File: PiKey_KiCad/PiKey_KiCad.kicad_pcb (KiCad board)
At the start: 2 copper layers, 22 x 42 mm, 1 part

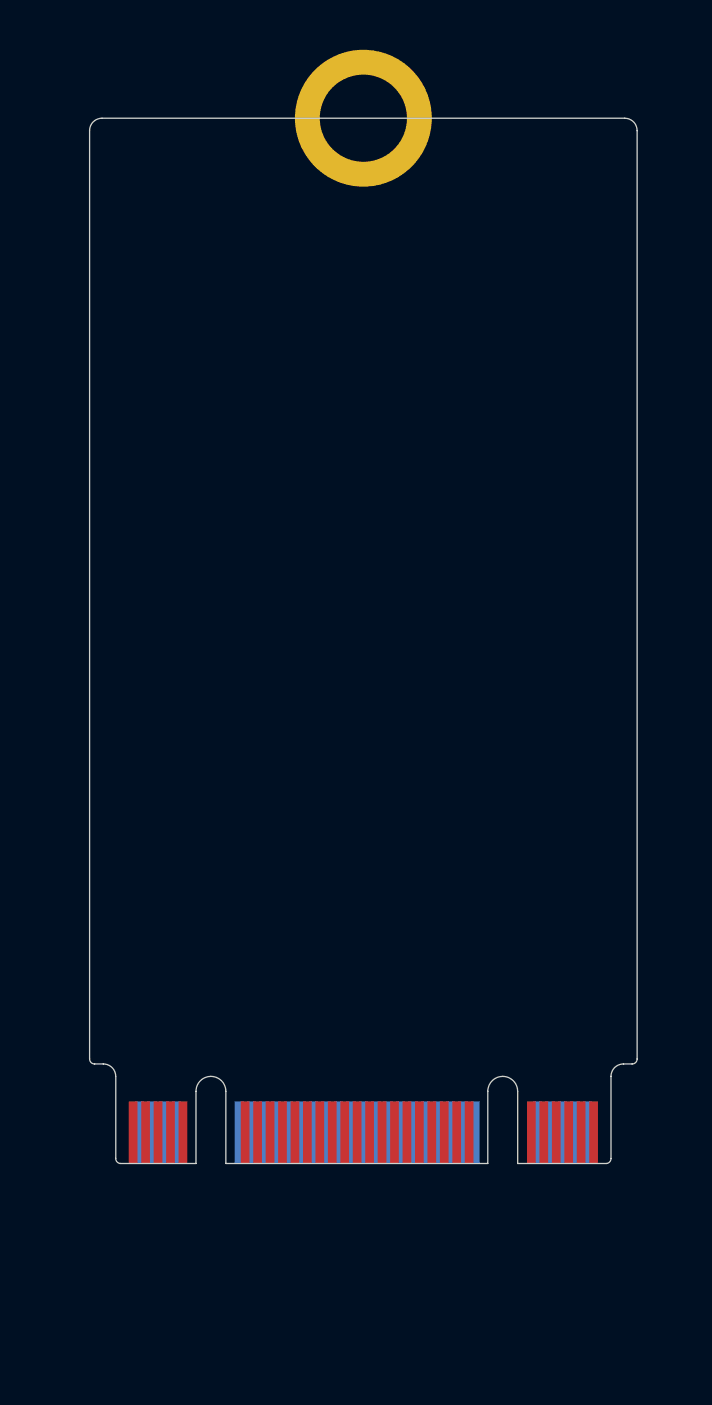
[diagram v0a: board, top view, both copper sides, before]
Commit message: Initial routing
Need to finish routing power and connecting GNDs together.
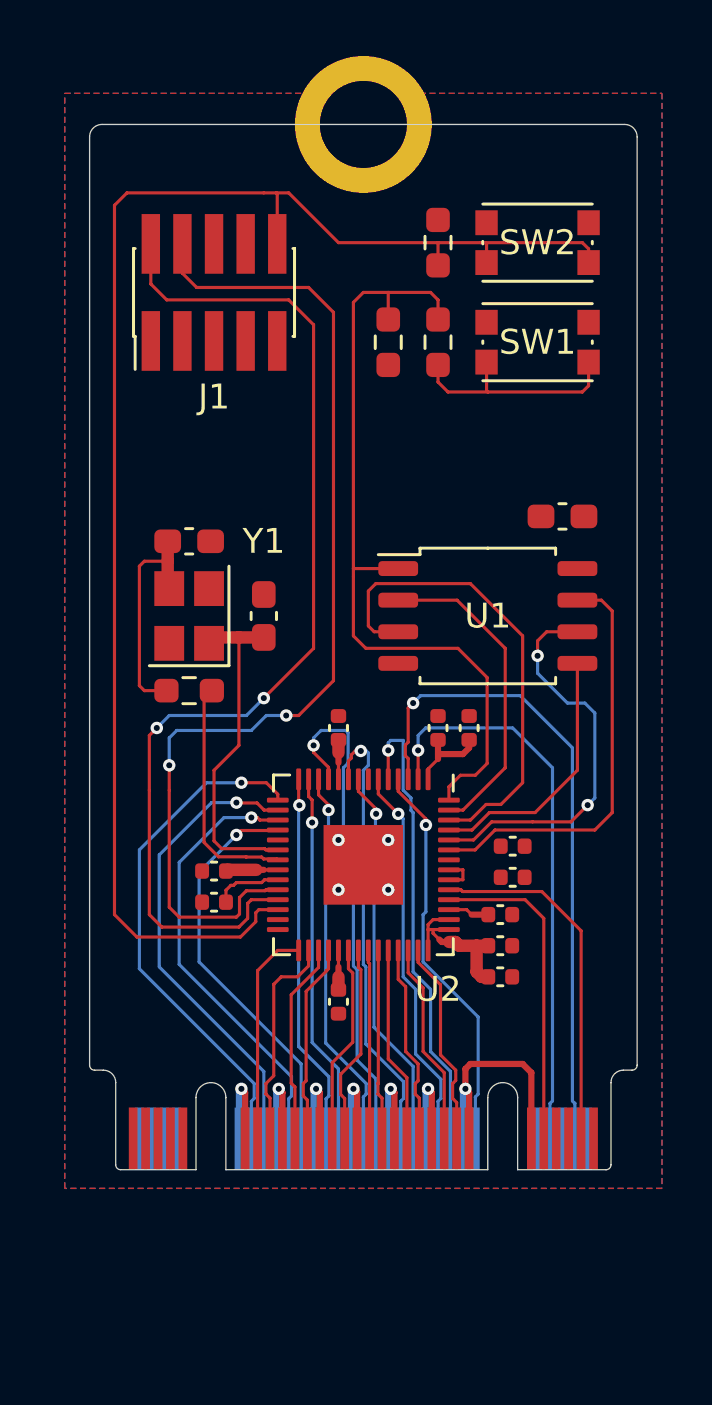
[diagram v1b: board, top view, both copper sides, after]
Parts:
- added C1: 100n, Capacitor_SMD:C_0603_1608Metric_Pad1.08x0.95mm_HandSolder, F.Cu at (158.0, 96.0)
- added C10: 100n, Capacitor_SMD:C_0402_1005Metric, F.Cu at (153.0, 104.5)
- added C11: 100n, Capacitor_SMD:C_0402_1005Metric, F.Cu at (155.5, 114.5)
- added C12: 100n, Capacitor_SMD:C_0402_1005Metric, F.Cu at (155.5, 113.2)
- added C13: 100n, Capacitor_SMD:C_0402_1005Metric, F.Cu at (156.0, 110.5)
- added C14: 100n, Capacitor_SMD:C_0402_1005Metric, F.Cu at (154.2, 104.5)
- added C2: 27p, Capacitor_SMD:C_0603_1608Metric_Pad1.08x0.95mm_HandSolder, F.Cu at (146.0, 100.0)
- added C3: 27p, Capacitor_SMD:C_0603_1608Metric_Pad1.08x0.95mm_HandSolder, F.Cu at (143.0, 97.0)
- added C4: 100n, Capacitor_SMD:C_0402_1005Metric, F.Cu at (156.0, 109.2)
- added C5: 100n, Capacitor_SMD:C_0402_1005Metric, F.Cu at (155.5, 112.0)
- added C6: 1u, Capacitor_SMD:C_0402_1005Metric, F.Cu at (144.0, 111.5)
- added C7: 1u, Capacitor_SMD:C_0402_1005Metric, F.Cu at (149.0, 115.5)
- added C8: 100n, Capacitor_SMD:C_0402_1005Metric, F.Cu at (144.0, 110.2)
- added C9: 100n, Capacitor_SMD:C_0402_1005Metric, F.Cu at (149.0, 104.5)
- added J1: SWD Header, Connector_PinHeader_1.27mm:PinHeader_2x05_P1.27mm_Vertical_SMD, F.Cu at (144.0, 87.0)
- added R1: 1K, Resistor_SMD:R_0603_1608Metric_Pad0.98x0.95mm_HandSolder, F.Cu at (153.0, 89.0)
- added R2: DNF, Resistor_SMD:R_0603_1608Metric_Pad0.98x0.95mm_HandSolder, F.Cu at (151.0, 89.0)
- added R3: 4k7, Resistor_SMD:R_0603_1608Metric_Pad0.98x0.95mm_HandSolder, F.Cu at (143.0, 103.0)
- added R4: 10K, Resistor_SMD:R_0603_1608Metric_Pad0.98x0.95mm_HandSolder, F.Cu at (153.0, 85.0)
- added SW1: BOOTSEL, Button_Switch_SMD:SW_Push_1P1T_NO_CK_KMR2, F.Cu at (157.0, 89.0)
- added SW2: RESET, Button_Switch_SMD:SW_Push_1P1T_NO_CK_KMR2, F.Cu at (157.0, 85.0)
- added U1: W25Q32JVSS, Package_SO:SOIC-8_5.23x5.23mm_P1.27mm, F.Cu at (155.0, 100.0)
- added U2: RP2040, Package_DFN_QFN:QFN-56-1EP_7x7mm_P0.4mm_EP3.2x3.2mm, F.Cu at (150.0, 110.0)
- added Y1: Crystal, Crystal:Crystal_SMD_SeikoEpson_FA238-4Pin_3.2x2.5mm, F.Cu at (143.0, 100.0)
- moved U$1 0.25 mm to (150.0, 122.2)
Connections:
- U$1 pad P$1: unconnected-(U$1-PadP$1) -> GND
- U$1 pad P$10: unconnected-(U$1-PadP$10) -> GND
- U$1 pad P$11: unconnected-(U$1-PadP$11) -> GND
- U$1 pad P$2: unconnected-(U$1-PadP$2) -> GND
- U$1 pad P$20: unconnected-(U$1-PadP$20) -> /GPIO2
- U$1 pad P$21: unconnected-(U$1-PadP$21) -> GND
- U$1 pad P$22: unconnected-(U$1-PadP$22) -> GND
- U$1 pad P$23: unconnected-(U$1-PadP$23) -> /A3
- U$1 pad P$24: unconnected-(U$1-PadP$24) -> /GPIO3
- U$1 pad P$25: unconnected-(U$1-PadP$25) -> /A2
- U$1 pad P$26: unconnected-(U$1-PadP$26) -> /GPIO4
- U$1 pad P$27: unconnected-(U$1-PadP$27) -> GND
- U$1 pad P$28: unconnected-(U$1-PadP$28) -> GND
- U$1 pad P$29: unconnected-(U$1-PadP$29) -> /A1
- U$1 pad P$3: unconnected-(U$1-PadP$3) -> /D+
- U$1 pad P$30: unconnected-(U$1-PadP$30) -> /GPIO6
- U$1 pad P$31: unconnected-(U$1-PadP$31) -> /A0
- U$1 pad P$32: unconnected-(U$1-PadP$32) -> /GPIO7
- U$1 pad P$33: unconnected-(U$1-PadP$33) -> GND
- U$1 pad P$34: unconnected-(U$1-PadP$34) -> GND
- U$1 pad P$35: unconnected-(U$1-PadP$35) -> /SCL
- U$1 pad P$36: unconnected-(U$1-PadP$36) -> /GPIO8
- U$1 pad P$37: unconnected-(U$1-PadP$37) -> /SDA
- U$1 pad P$38: unconnected-(U$1-PadP$38) -> /GPIO9
- U$1 pad P$39: unconnected-(U$1-PadP$39) -> GND
- U$1 pad P$4: unconnected-(U$1-PadP$4) -> /RX
- U$1 pad P$40: unconnected-(U$1-PadP$40) -> GND
- U$1 pad P$41: unconnected-(U$1-PadP$41) -> /GPIO23
- U$1 pad P$42: unconnected-(U$1-PadP$42) -> /GPIO10
- U$1 pad P$43: unconnected-(U$1-PadP$43) -> /GPIO22
- U$1 pad P$44: unconnected-(U$1-PadP$44) -> /GPIO11
- U$1 pad P$45: unconnected-(U$1-PadP$45) -> GND
- U$1 pad P$46: unconnected-(U$1-PadP$46) -> GND
- U$1 pad P$47: unconnected-(U$1-PadP$47) -> /GPIO21
- U$1 pad P$48: unconnected-(U$1-PadP$48) -> /GPIO15
- U$1 pad P$49: unconnected-(U$1-PadP$49) -> /MISO
- U$1 pad P$5: unconnected-(U$1-PadP$5) -> GND
- U$1 pad P$50: unconnected-(U$1-PadP$50) -> /GPIO14
- U$1 pad P$51: unconnected-(U$1-PadP$51) -> GND
- U$1 pad P$52: unconnected-(U$1-PadP$52) -> GND
- U$1 pad P$53: unconnected-(U$1-PadP$53) -> /MOSI
- U$1 pad P$54: unconnected-(U$1-PadP$54) -> /GPIO13
- U$1 pad P$55: unconnected-(U$1-PadP$55) -> /SCK
- U$1 pad P$56: unconnected-(U$1-PadP$56) -> /GPIO12
- U$1 pad P$57: unconnected-(U$1-PadP$57) -> GND
- U$1 pad P$58: unconnected-(U$1-PadP$58) -> GND
- U$1 pad P$6: unconnected-(U$1-PadP$6) -> GND
- U$1 pad P$67: unconnected-(U$1-PadP$67) -> +3V3
- U$1 pad P$68: unconnected-(U$1-PadP$68) -> GND
- U$1 pad P$69: unconnected-(U$1-PadP$69) -> +3V3
- U$1 pad P$7: unconnected-(U$1-PadP$7) -> GND
- U$1 pad P$70: unconnected-(U$1-PadP$70) -> /GPIO17
- U$1 pad P$71: unconnected-(U$1-PadP$71) -> GND
- U$1 pad P$72: unconnected-(U$1-PadP$72) -> /GPIO16
- U$1 pad P$73: unconnected-(U$1-PadP$73) -> GND
- U$1 pad P$74: unconnected-(U$1-PadP$74) -> GND
- U$1 pad P$75: unconnected-(U$1-PadP$75) -> GND
- U$1 pad P$8: unconnected-(U$1-PadP$8) -> /TX
- U$1 pad P$9: unconnected-(U$1-PadP$9) -> /D-
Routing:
- net /RUN: track 0.00 -> 60.6 mm
- net /SWDIO: track 0.00 -> 43.3 mm, vias 0 -> 2
- net /SWDCLK: track 0.00 -> 42.4 mm, vias 0 -> 2
- net GND: track 0.00 -> 35.2 mm, vias 0 -> 11
- net /FLASH_CS: track 0.00 -> 32.7 mm
- net /RX: track 0.00 -> 26.4 mm, vias 0 -> 1
- net /TX: track 0.00 -> 22.9 mm, vias 0 -> 1
- net /GPIO12: track 0.00 -> 20.7 mm, vias 0 -> 1
- net /GPIO8: track 0.00 -> 20.4 mm, vias 0 -> 1
- net /QSPI_SD2: track 0.00 -> 19.4 mm
- net /GPIO13: track 0.00 -> 18.9 mm, vias 0 -> 1
- net /GPIO3: track 0.00 -> 18.9 mm, vias 0 -> 1
- net /GPIO7: track 0.00 -> 18.1 mm, vias 0 -> 1
- net /GPIO14: track 0.00 -> 17.8 mm, vias 0 -> 1
- net +3V3: track 0.00 -> 17.2 mm
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- added copper zone on B.Cu, net GND
- added copper zone on F.Cu, net GND
- added copper zone on In1.Cu, net GND
- added copper zone on In2.Cu, net GND
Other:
- copper layers 2 -> 4

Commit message: Delay matching and stitching vias
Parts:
- moved C11 0.50 mm to (156.0, 114.5)
- moved C12 0.50 mm to (156.0, 113.2)
- moved C2 0.50 mm to (146.5, 100.0)
- moved C3 0.50 mm to (143.0, 96.5)
- moved C5 0.50 mm to (156.0, 112.0)
- moved R3 0.50 mm to (143.0, 103.5)
- moved C7 0.25 mm to (149.0, 115.8)
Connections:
- U$1 pad P$6: GND -> /TX
- U$1 pad P$70: /GPIO17 -> GND
- U$1 pad P$72: /GPIO16 -> GND
- U$1 pad P$8: /TX -> GND
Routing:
- net +3V3: track 17.2 -> 128.7 mm, vias 0 -> 12
- net +1V1: track 4.40 -> 18.8 mm
- net /QSPI_SD0: track 10.5 -> 20.0 mm
- net /QSPI_SD1: track 12.9 -> 19.9 mm
- net GND: track 35.2 -> 39.6 mm, vias 11 -> 57
- net /QSPI_SD3: track 16.9 -> 20.0 mm
- net /D-: track 13.0 -> 16.0 mm
- net /D+: track 14.3 -> 16.0 mm
- net /GPIO8: track 20.4 -> 21.8 mm
- net /SWDIO: track 43.3 -> 44.2 mm
- net /XOUT_R: track 9.12 -> 10.1 mm
- net /RX: track 26.4 -> 27.2 mm
- net /SWDCLK: track 42.4 -> 43.1 mm
- net /QSPI_SD2: track 19.4 -> 20.0 mm
- net /XIN: track 13.6 -> 14.1 mm

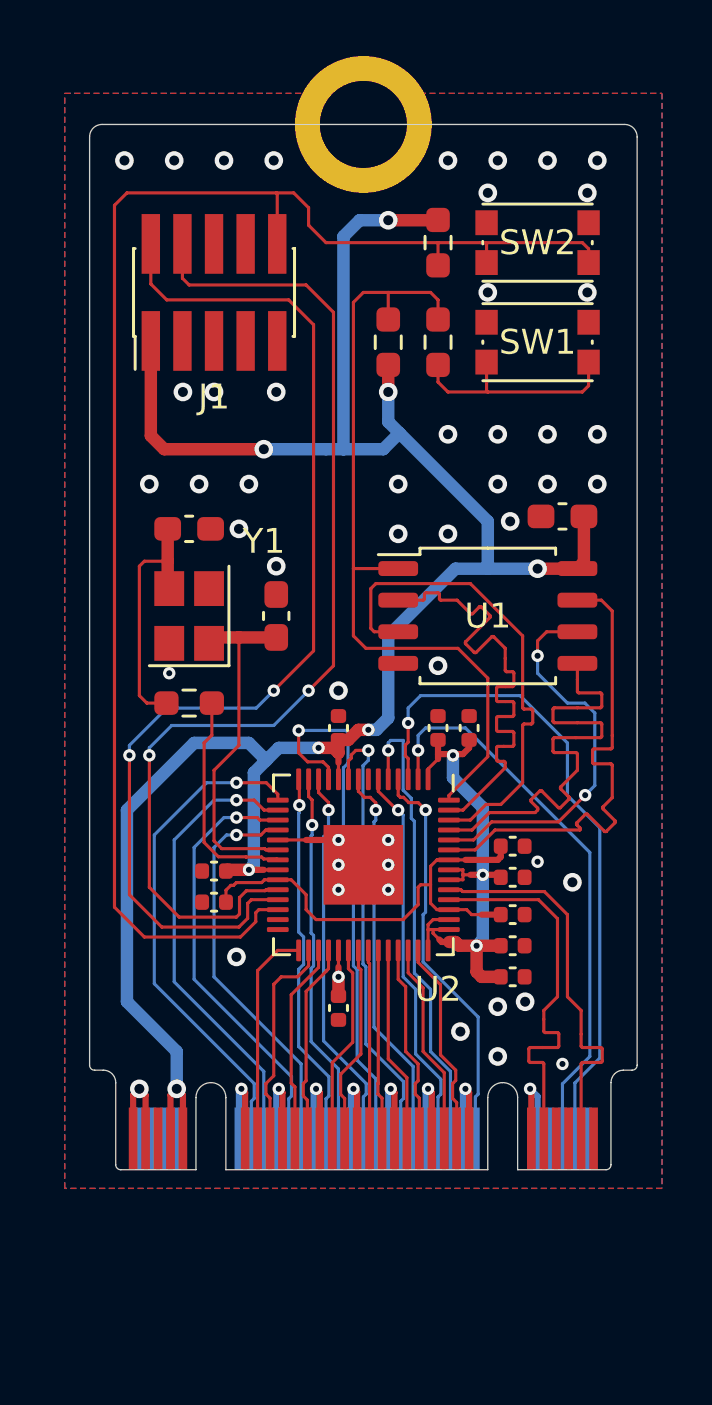
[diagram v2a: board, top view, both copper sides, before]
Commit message: Redid M.2 signals on back
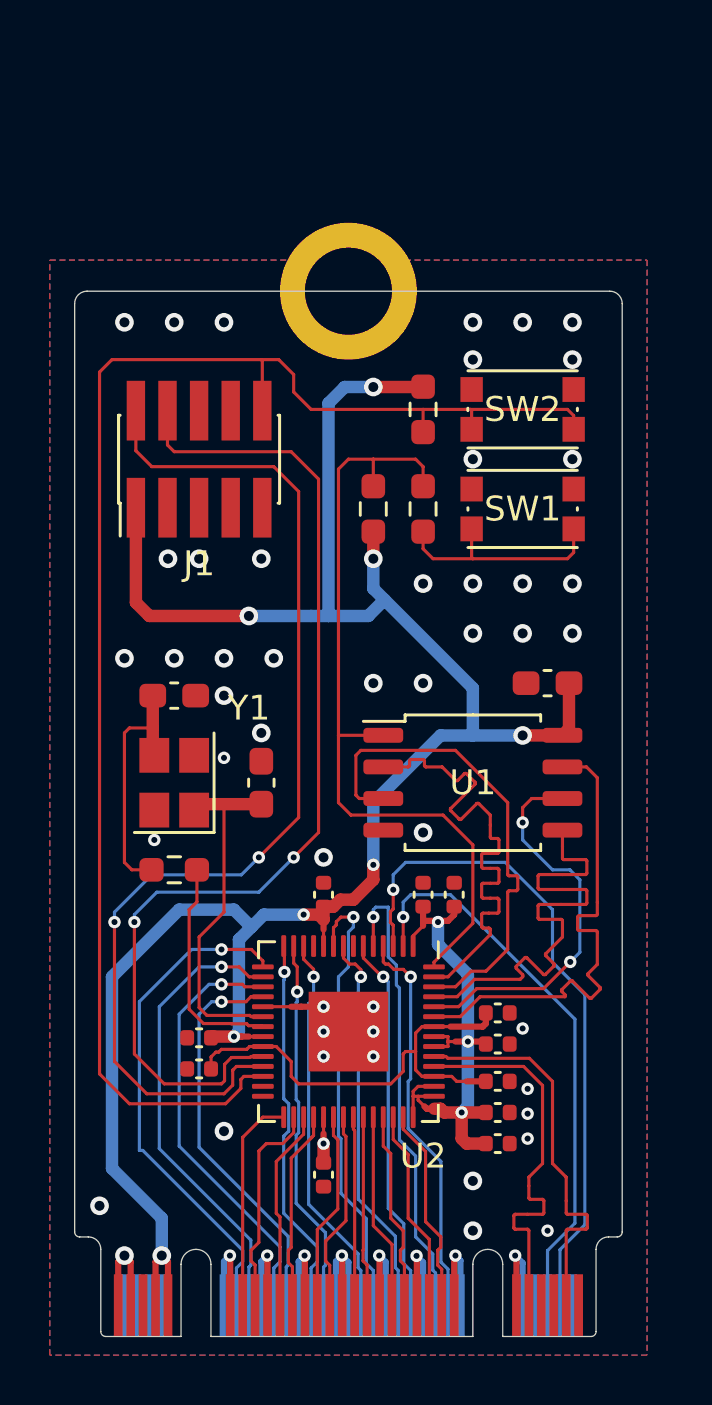
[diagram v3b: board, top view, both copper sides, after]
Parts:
- moved C1 6.73 mm to (157.4, 102.7)
- moved C10 6.73 mm to (152.4, 111.2)
- moved C11 6.73 mm to (155.4, 121.2)
- moved C12 6.73 mm to (155.4, 120.0)
- moved C13 6.73 mm to (155.4, 117.2)
- moved C14 6.73 mm to (153.7, 111.2)
- moved C2 6.73 mm to (145.9, 106.7)
- moved C3 6.73 mm to (142.4, 103.2)
- moved C4 6.73 mm to (155.4, 116.0)
- moved C5 6.73 mm to (155.4, 118.7)
- moved C6 6.73 mm to (143.4, 118.2)
- moved C7 6.73 mm to (148.4, 122.5)
- moved C8 6.73 mm to (143.4, 117.0)
- moved C9 6.73 mm to (148.4, 111.2)
- moved J1 6.73 mm to (143.4, 93.7)
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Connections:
- U$1 pad P$20: /GPIO2 -> GND
- U$1 pad P$22: GND -> /GPIO2
- U$1 pad P$26: /GPIO4 -> GND
- U$1 pad P$28: GND -> /GPIO4
- U$1 pad P$32: /GPIO7 -> GND
- U$1 pad P$34: GND -> /GPIO7
- U$1 pad P$36: /GPIO8 -> /GPIO9
- U$1 pad P$38: /GPIO9 -> GND
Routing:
- net /GPIO8: track 21.8 -> 0.00 mm, vias 1 -> 0
- net GND: track 39.6 -> 41.6 mm, vias 57 -> 56
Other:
- outline, holes or cut-outs redrawn

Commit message: Improved silkscreen
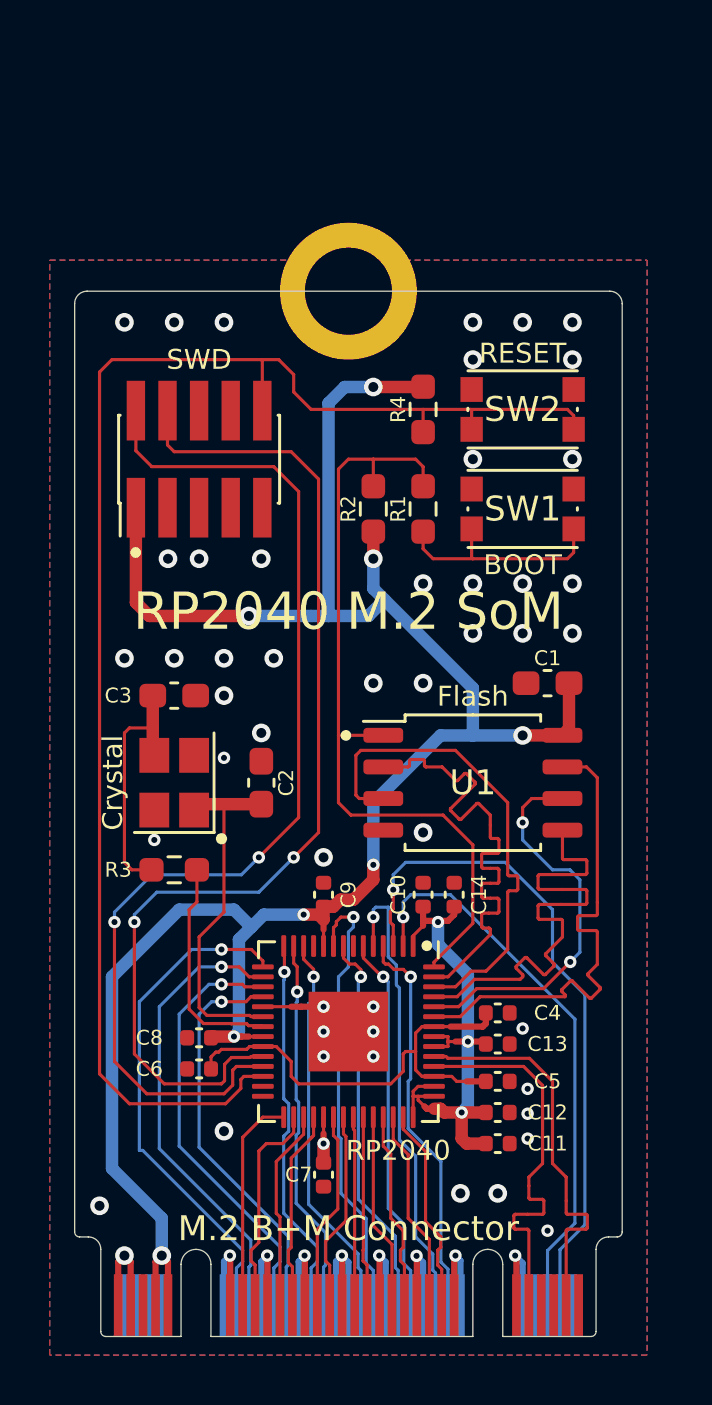
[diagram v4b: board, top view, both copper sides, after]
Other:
- board text added: "BOOT"
- board text added: "Crystal"
- board text added: "Flash"
- board text added: "M.2 B+M Connector"
- board text added: "RESET"
- board text added: "RP2040"
- board text added: "RP2040 M.2 SoM"
- board text added: "SWD"
